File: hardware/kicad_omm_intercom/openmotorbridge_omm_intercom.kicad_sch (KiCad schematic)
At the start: 5 parts, among them J1 TYPE-C-31-M-12_IP67, U2 BQ24075RGTR, U4 ES8388

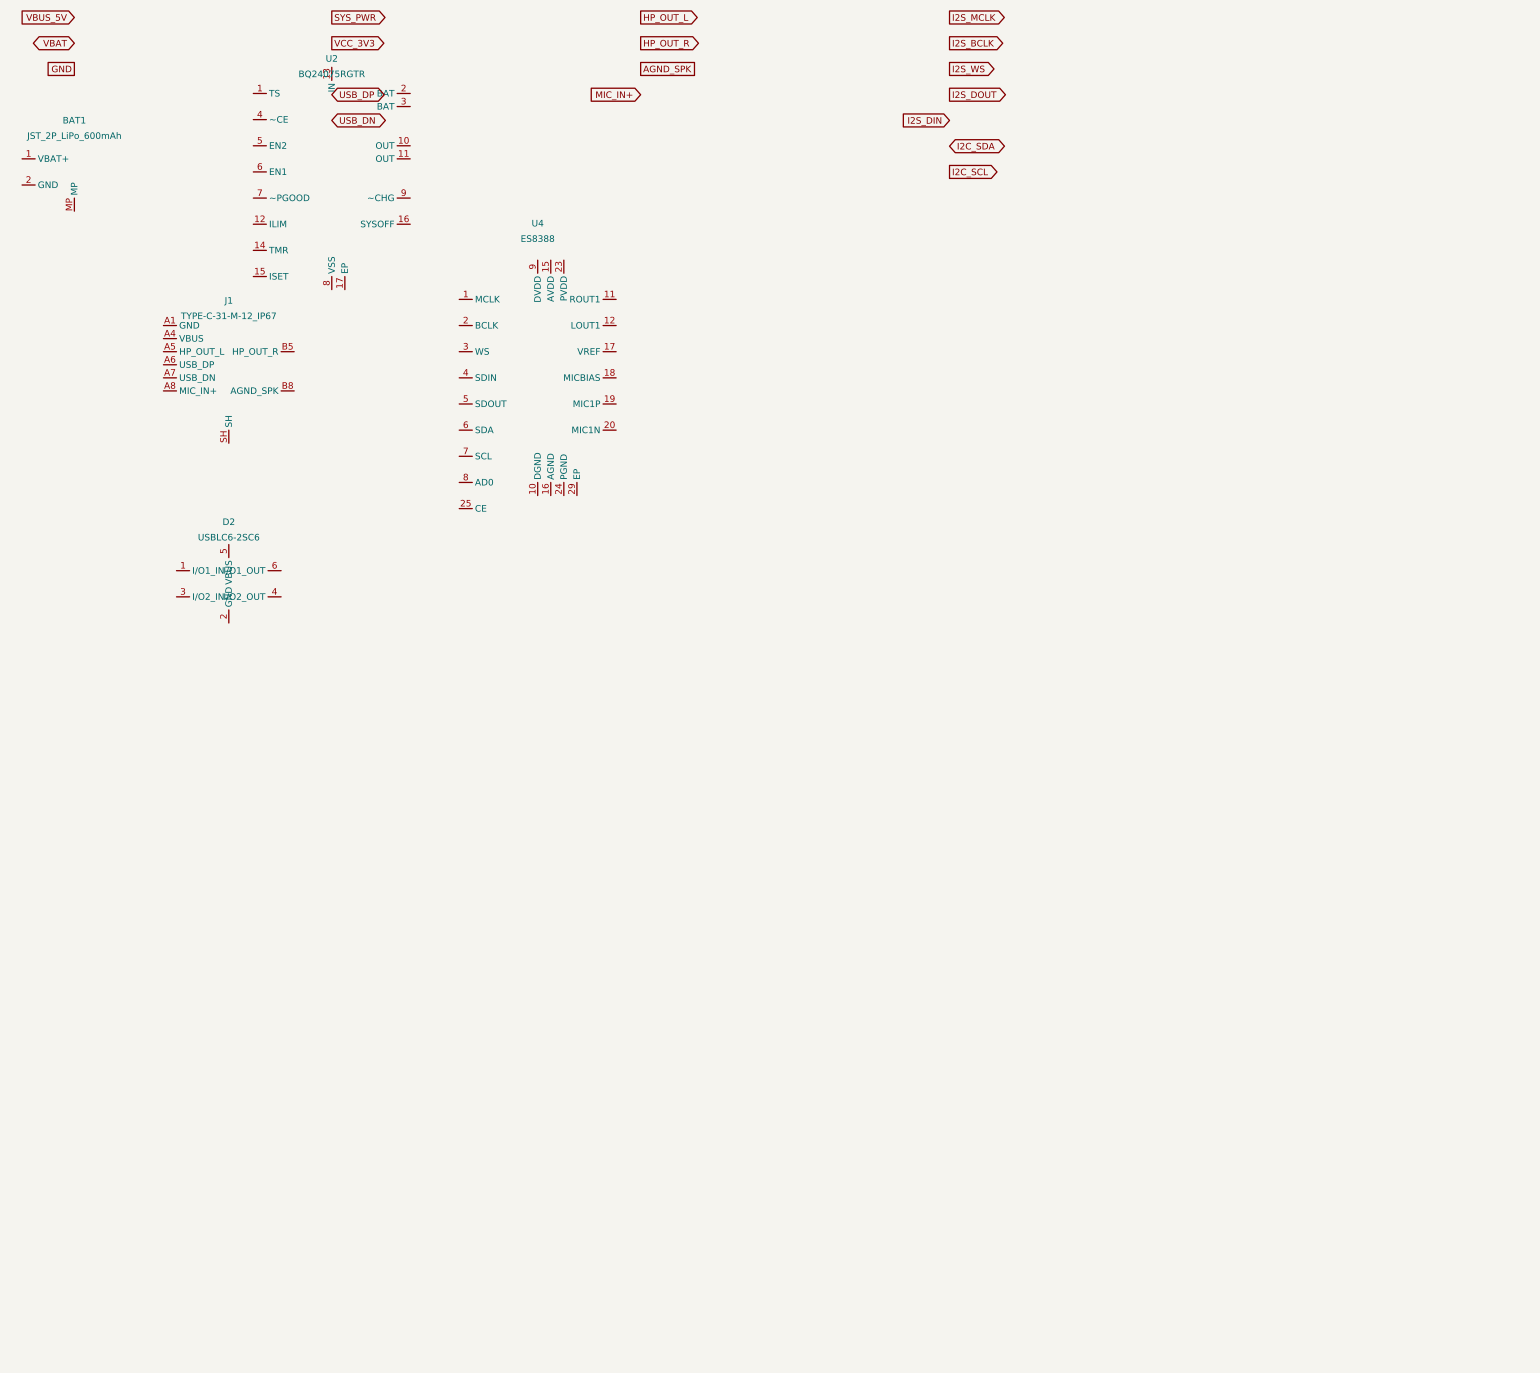
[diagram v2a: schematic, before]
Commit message: feat(hw,docs): implement Dual-Engine OMB Lite architecture for PCBA 09 and PCBA 10
- Schematic: Add ESP32-PICO-V3-02 (BT Classic/BLE co-processor) and Johanson 2450AT18 chip antenna
- PCB: Add Grobplatzierung and Vorverbindung nets on B.Cu for PCBA 09 and PCBA 10
- Firmware: Add co-processor UART link config and disable BT on C6 to eliminate CoEx time-slicing
- Documentation: Add Dual-Engine architecture, Cardo DMC Bridge / Sena Bridge, and Profile C OMB Lite
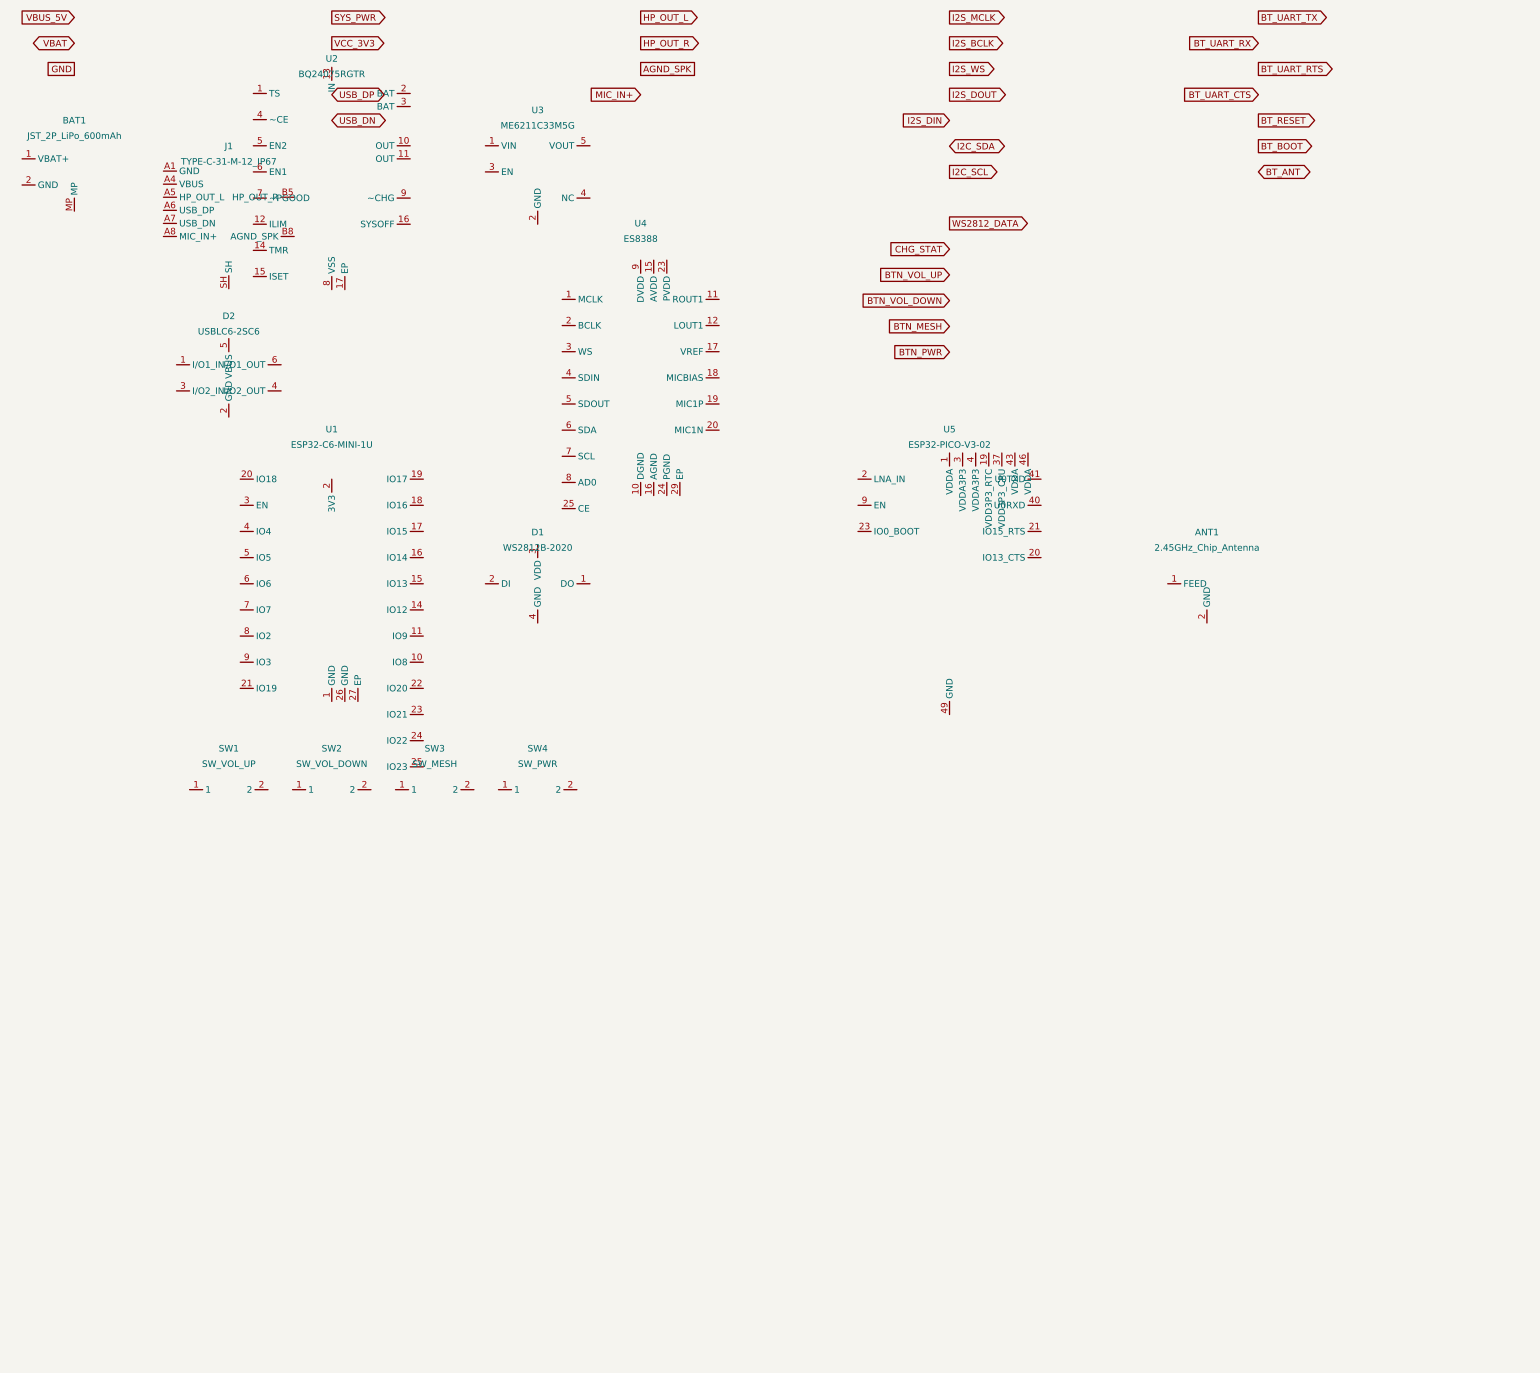
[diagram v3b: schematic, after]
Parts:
- added ANT1: 2.45GHz_Chip_Antenna, RF_Antenna:Johanson_2450AT18x100, symbol RF_Antenna:Johanson_2450AT18x100
- added D1: WS2812B-2020, LED_SMD:LED_WS2812B-2020_PLCC4_2.0x2.0mm, symbol LED:WS2812B-2020
- added SW1: SW_VOL_UP, Button_Switch_SMD:SW_Push_SPST_NO_Alps_SKRK, symbol Switch:SW_Push_SPST
- added SW2: SW_VOL_DOWN, Button_Switch_SMD:SW_Push_SPST_NO_Alps_SKRK, symbol Switch:SW_Push_SPST
- added SW3: SW_MESH, Button_Switch_SMD:SW_Push_SPST_NO_Alps_SKRK, symbol Switch:SW_Push_SPST
- added SW4: SW_PWR, Button_Switch_SMD:SW_Push_SPST_NO_Alps_SKRK, symbol Switch:SW_Push_SPST
- added U1: ESP32-C6-MINI-1U, RF_Module:ESP32-C6-MINI-1U, symbol MCU:ESP32-C6-MINI-1U
- added U3: ME6211C33M5G, Package_TO_SOT_SMD:SOT-23-5, symbol Regulator:ME6211C33M5G
- added U5: ESP32-PICO-V3-02, Package_DFN_QFN:QFN-48-1EP_7x7mm_P0.5mm_EP5.3x5.3mm, symbol MCU:ESP32-PICO-V3-02
- BAT1: LCSC (none) -> C160402
- D2: LCSC (none) -> C7519
- J1: LCSC (none) -> C2836262
- U2: LCSC (none) -> C96825
- U4: LCSC (none) -> C365736
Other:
- title: OpenMotorBridge OMM 2.4 GHz Intercom & UCS Modul (PCBA 09) -> OpenMotorBridge OMM 2.4 GHz Intercom & UCS Modul (PCBA 09) - Dual-Engine

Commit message: feat(omm): set compact stubby antenna as helmet default, add internal J_HELMET audio & maintain external USB-C
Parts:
- added J_HELMET: HELMET_AUDIO_6P, Connector_JST:JST_SH_SM06B-SRSS-TB_1x06-1MP_P1.00mm_Horizontal, symbol Connector:Conn_01x06_Pin
- added J_RF: U.FL-R-SMT-1, Connector_Coaxial:U.FL_Hirose_U.FL-R-SMT-1_Vertical, symbol Connector:U.FL-R-SMT
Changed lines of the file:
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@@
 		(pin "2")
 	)
+	(symbol (lib_id "Connector:Conn_01x06_Pin") (at 160.0 180.0 0) (unit 1)
+		(in_bom yes) (on_board yes) (dnp no)
+		(property "Reference" "J_HELMET" (at 160.0 165.0 0) (effects (font (size 1.27 1.27))))
+		(property "Value" "HELMET_AUDIO_6P" (at 160.0 168.0 0) (effects (font (size 1.27 1.27))))
+		(property "Footprint" "Connector_JST:JST_SH_SM06B-SRSS-TB_1x06-1MP_P1.00mm_Horizontal" (at 0 0 0) (effects (font (size 1.27 1.27)) hide))
+		(property "LCSC" "C136657" (at 0 0 0) (effects (font (size 1.27 1.27)) hide))
+		(pin "1")
+		(pin "2")
+		(pin "3")
+		(pin "4")
+		(pin "5")
+		(pin "6")
+	)
+	(symbol (lib_id "Connector:U.FL-R-SMT") (at 200.0 180.0 0) (unit 1)
+		(in_bom yes) (on_board yes) (dnp no)
+		(property "Reference" "J_RF" (at 200.0 165.0 0) (effects (font (size 1.27 1.27))))
+		(property "Value" "U.FL-R-SMT-1" (at 200.0 168.0 0) (effects (font (size 1.27 1.27))))
+		(property "Footprint" "Connector_Coaxial:U.FL_Hirose_U.FL-R-SMT-1_Vertical" (at 0 0 0) (effects (font (size 1.27 1.27)) hide))
+		(property "LCSC" "C14899" (at 0 0 0) (effects (font (size 1.27 1.27)) hide))
+		(pin "1")
+		(pin "2")
+		(pin "3")
+	)
 )

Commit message: fix(omm): align CAD, BOM and CPL with user re-routed PCBA 09 J_HELMET position opposite USB-C
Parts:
- removed J_RF: U.FL-R-SMT-1, Connector_Coaxial:U.FL_Hirose_U.FL-R-SMT-1_Vertical, symbol Connector:U.FL-R-SMT
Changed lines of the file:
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@@
 		(pin "6")
 	)
-	(symbol (lib_id "Connector:U.FL-R-SMT") (at 200.0 180.0 0) (unit 1)
-		(in_bom yes) (on_board yes) (dnp no)
-		(property "Reference" "J_RF" (at 200.0 165.0 0) (effects (font (size 1.27 1.27))))
-		(property "Value" "U.FL-R-SMT-1" (at 200.0 168.0 0) (effects (font (size 1.27 1.27))))
-		(property "Footprint" "Connector_Coaxial:U.FL_Hirose_U.FL-R-SMT-1_Vertical" (at 0 0 0) (effects (font (size 1.27 1.27)) hide))
-		(property "LCSC" "C14899" (at 0 0 0) (effects (font (size 1.27 1.27)) hide))
-		(pin "1")
-		(pin "2")
-		(pin "3")
-	)
 )

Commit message: fix(hardware): fleet-wide 7-PCBA remediation, schematic parity & doc alignment
- PCBA 01 (Central Box): Synchronized DTM-12 schematic and PCB routing, purged obsolete analog audio transformers/HD26 connector.
- PCBA 03 (Smart Cartridge): Verified Kelvin ground isolation on J_AUDIO_PWR, resolved U1.16 BAY_SELECT single net.
- PCBA 05 (Front Node): Mapped DW3110 UWB SPI/IRQ/RST to ESP32-S3 pads 30-35, connected MK1 I2S MEMS mic and Y_UWB crystal.
- PCBA 07 (Smart Keyfob): Connected 12 unrouted signals (SX1262 LoRa SPI, DRV2605L I2C, SWD, RTC crystal, buttons) to nRF52840 pads.
- PCBA 08 (Radar Sub-MCU): Synchronized J1.1 power rail to VCC_5V, connected Y1_UWB crystal to DW3110 pads 4 & 5.
- PCBA 09 & PCBA 10 (OMM 2.4 GHz & 446 MHz): Verified 4-layer stackup, BQ24075 ground ties, SA818 isolation, and vertical B.Cu J_HELMET orientation.
- Tools: Added verify_hardware_integrity.py with automated DRC/parity/single-net/floating-pad checks (all 7 PCBAs HEALTHY).
- Docs: Synchronized docs/de and docs/en hardware specifications, pinouts, and DTM-12 architecture.
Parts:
- added H1, H2, H3, H4: M2_MountingHole, MountingHole_2.2mm_M2_Pad, symbol Mechanical:MountingHole_Pad
- BAT1: footprint Connector_JST:JST_SH_BM02B-SRSS-TB_1x02-1MP_P1.00mm_Vertical -> JST_SH_BM02B-SRSS-TB_1x02-1MP_P1.00mm_Vertical
- D1: footprint LED_SMD:LED_WS2812B-2020_PLCC4_2.0x2.0mm -> LED_WS2812B-2020_PLCC4_2.0x2.0mm
- D2: footprint Package_TO_SOT_SMD:SOT-23-6 -> SOT-23-6
- J1: footprint Connector_USB:USB_C_Receptacle_HRO_TYPE-C-31-M-12 -> USB_C_Receptacle_HRO_TYPE-C-31-M-12
- J_HELMET: footprint Connector_JST:JST_SH_SM06B-SRSS-TB_1x06-1MP_P1.00mm_Horizontal -> JST_SH_BM06B-SRSS-TB_1x06-1MP_P1.00mm_Vertical
- SW1: value SW_VOL_UP -> SW_1; footprint Button_Switch_SMD:SW_Push_SPST_NO_Alps_SKRK -> SW_Push_SPST_NO_Alps_SKRK
- SW2: value SW_VOL_DOWN -> SW_2; footprint Button_Switch_SMD:SW_Push_SPST_NO_Alps_SKRK -> SW_Push_SPST_NO_Alps_SKRK
- SW3: value SW_MESH -> SW_3; footprint Button_Switch_SMD:SW_Push_SPST_NO_Alps_SKRK -> SW_Push_SPST_NO_Alps_SKRK
- SW4: value SW_PWR -> SW_4; footprint Button_Switch_SMD:SW_Push_SPST_NO_Alps_SKRK -> SW_Push_SPST_NO_Alps_SKRK
- U1: footprint RF_Module:ESP32-C6-MINI-1U -> ESP32-S2-MINI-1U
- U2: footprint Package_DFN_QFN:VQFN-16-1EP_3x3mm_P0.5mm_EP1.8x1.8mm -> VQFN-16-1EP_3x3mm_P0.5mm_EP1.8x1.8mm
- U3: footprint Package_TO_SOT_SMD:SOT-23-5 -> SOT-23
- U4: footprint Package_DFN_QFN:QFN-28-1EP_4x4mm_P0.4mm_EP2.4x2.4mm -> QFN-28-1EP_4x4mm_P0.4mm_EP2.4x2.4mm
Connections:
- net AGND_SPK: now also J_HELMET.3 (Pin_3), U4.24 (PGND)
- net BT_ANT: now also ANT1.1 (FEED), U5.2 (LNA_IN)
- net BT_BOOT: now also U1.12 (IO10), U5.23 (IO0_BOOT)
- net BT_RESET: now also U1.13 (IO11), U5.9 (EN)
- net BT_UART_CTS: now also U1.26 (IO24_CTS), U5.20 (IO13_CTS)
- net BT_UART_RTS: now also U1.27 (IO25_RTS), U5.21 (IO15_RTS)
- net BT_UART_RX: now also U1.29 (IO1), U5.40 (U0RXD)
- net BT_UART_TX: now also U1.28 (IO0), U5.41 (U0TXD)
- net CHG_STAT: now also U1.7 (IO7), U2.9 (~CHG)
- net GND: now also ANT1.2 (GND), BAT1.2 (-), BAT1.MP, D1.1 (DO), D1.3 (VDD), D2.2 (GND), J1.A1 (GND), J1.A12 (GND), J1.A5 (HP_OUT_L), J1.B1 (GND), J1.B12 (GND), J1.B5 (HP_OUT_R), J1.SH, J_HELMET.MP, SW1.2, SW2.2, SW3.2, SW4.2, U1.1 (GND), U1.3 (EN), U1.40 (GND), U1.41 (GND), U1.42 (GND), U1.43 (GND), U1.44 (GND), U1.45 (GND), U1.46 (GND), U1.47 (GND), U1.48 (GND), U1.49 (GND), U1.50 (GND), U1.51 (GND), U1.52 (GND), U1.53 (GND), U1.54 (GND), U1.55 (GND), U1.56 (GND), U1.57 (GND), U1.58 (GND), U1.59 (GND), U1.60 (GND), U1.61 (GND), U1.62 (GND), U1.63 (GND), U1.64 (GND), U1.65 (GND), U2.1 (TS), U2.12 (ILIM), U2.14 (TMR), U2.15 (ISET), U2.16 (SYSOFF), U2.17 (EP), U2.4 (~CE), U2.5 (EN2), U2.6 (EN1), U2.7 (~PGOOD), U2.8 (VSS), U3.1 (GND), U4.10 (DGND), U4.29 (EP), U4.8 (AD0), U5.49 (GND), H1.1, H2.1, H3.1, H4.1
- net I2C_SCL: now also U1.11 (IO9), U4.7 (SCL)
- net I2C_SDA: now also U1.10 (IO8), U4.6 (SDA)
- net I2S_BCLK: now also U1.22 (IO20), U4.2 (BCLK)
- net I2S_DIN: now also U1.25 (IO23), U4.5 (SDOUT)
- net I2S_DOUT: now also U1.24 (IO22), U4.4 (SDIN)
- net I2S_MCLK: now also U1.21 (IO19), U4.1 (MCLK)
- net I2S_WS: now also U1.23 (IO21), U4.3 (WS)
- net SYS_PWR: now also U2.10 (OUT), U2.11 (OUT), U3.3 (VIN)
- net USB_DN: now also D2.3 (I/O2_IN), D2.4 (I/O2_OUT), J1.A7 (USB_DN), J1.B7 (USB_DN), U1.14 (IO12)
- net USB_DP: now also D2.1 (I/O1_IN), D2.6 (I/O1_OUT), J1.A6 (USB_DP), J1.B6 (USB_DP), U1.15 (IO13)
- net VBAT: now also BAT1.1 (+), U2.2 (BAT), U2.3 (BAT)
- net VBUS_5V: now also D2.5 (VBUS), J1.A4 (VBUS), J1.A9 (VBUS), J1.B4 (VBUS), J1.B9 (VBUS), U2.13 (IN)
- net VCC_3V3: now also D1.2 (DI), U1.2 (3V3), U3.2 (VOUT), U4.15 (AVDD), U4.23 (PVDD), U4.25 (CE), U4.9 (DVDD), U5.1 (VDDA), U5.19 (VDD3P3_RTC), U5.3 (VDDA3P3), U5.37 (VDD3P3_CPU), U5.4 (VDDA3P3), U5.43 (VDDA), U5.46 (VDDA)
- net WS2812_DATA: now also D1.4 (GND), U1.6 (IO6)
- net AUDIO_OUT_R: now reaches U4.11 (ROUT1)
- net AUDIO_OUT_R: now also J_HELMET.2 (Pin_2)
- net AUDIO_OUT_L: now reaches U4.12 (LOUT1)
- net AUDIO_OUT_L: now also J_HELMET.1 (Pin_1)
- net AGND: now reaches U4.16 (AGND)
- net AGND: now also U4.17 (VREF), U4.18 (MICBIAS)
- net VOICE_IN: now reaches U4.19 (MIC1P)
- net VOICE_IN: now also J_HELMET.4 (Pin_4)
- net AGND_MIC: now reaches U4.20 (MIC1N)
- net AGND_MIC: now also J_HELMET.5 (Pin_5)
- net BTN_2: now reaches SW2.1
- net BTN_2: now also U1.9 (IO3)
- net BTN_3: now reaches SW3.1
- net BTN_3: now also U1.4 (IO4)
- net BTN_4: now reaches U1.5 (IO5)
- net BTN_4: now also SW4.1
- net BTN_1: now reaches U1.8 (IO2)
- net BTN_1: now also J_HELMET.6 (Pin_6), SW1.1
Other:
- moved on the sheet: BAT1, D1, D2, SW1, SW2, SW3, SW4, U2
